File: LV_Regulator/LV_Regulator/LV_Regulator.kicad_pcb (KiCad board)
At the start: 4 copper layers, 150 x 100 mm, 190 parts, among them IC1 UCC12040DVE, IC2 MIC29152WU, IC3 MIC29152WU, J3 430450800, K1 41.52.9.005.0010, K1 REL, Q1 BC807, U1 ADM2483xRW, U2 STM32F103C8Tx, U3 25CSM04xxSN, U4 BQ25858QWRRVRQ1, U5 CSD19506KTT, U6 CSD19506KTT, U7 CSD19506KTT, U8 CSD19506KTT, Y1 32.768kHz, Y2 8MHz

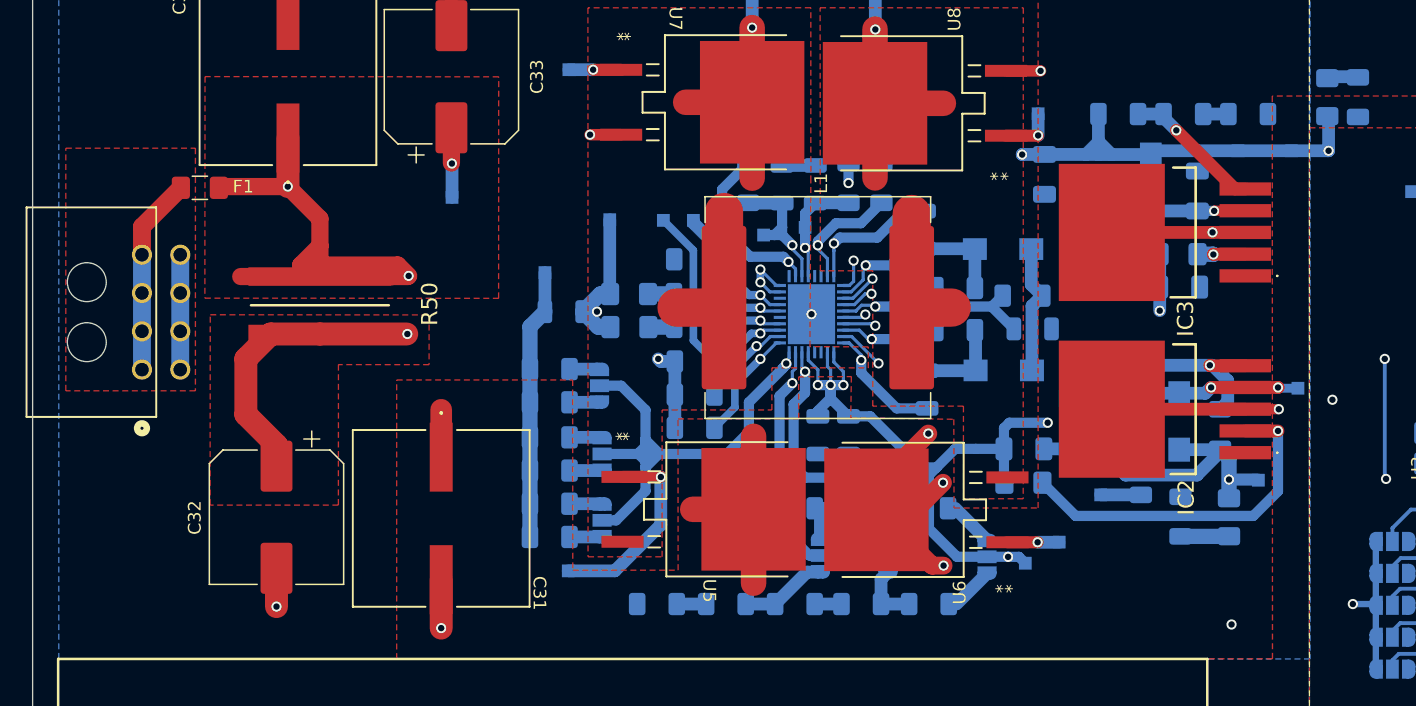
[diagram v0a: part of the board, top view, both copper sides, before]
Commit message: Fixed DRC & some other minor tweaks
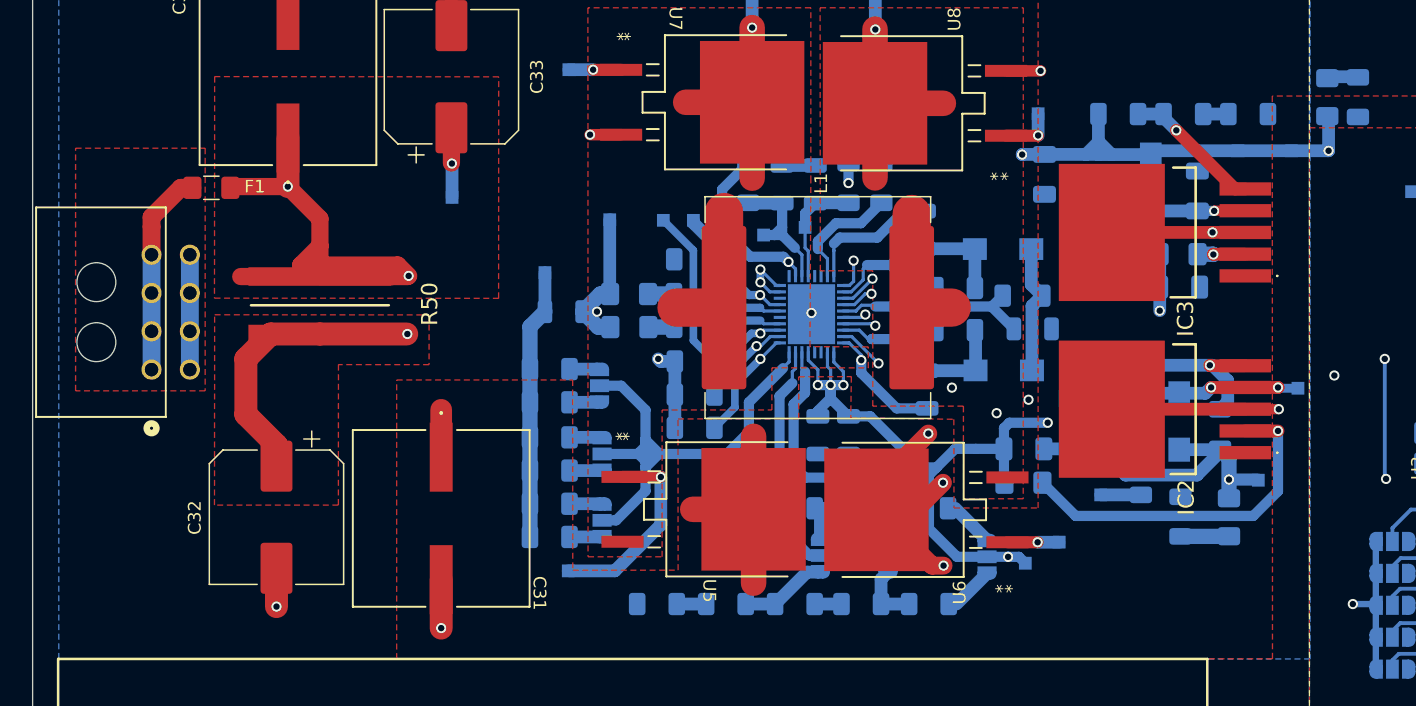
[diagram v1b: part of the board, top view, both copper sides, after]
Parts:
- moved F1 0.90 mm to (95.0, 75.1)
- moved J3 0.75 mm to (90.3, 89.3)
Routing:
- net CE_N: track 102.7 -> 93.9 mm
- net VOUT: track 67.9 -> 67.0 mm
- net Net-(F1-Pad2): track 15.5 -> 16.1 mm
- net I2C_SCL: track 82.9 -> 83.4 mm, vias 2 -> 4
- net BTST2: track 9.36 -> 9.34 mm, vias 1 -> 0
- net Izbor_frekvencije: vias 1 -> 0
- net SRN: vias 1 -> 0
- net SW2: vias 2 -> 1
- net SRP: vias 1 -> 0
- net Net-(U4-STAT): vias 1 -> 0
- net Net-(U4-PG_N): vias 1 -> 0
- net Net-(U4-MODE): vias 1 -> 0
- net DRV_SUPPLY: vias 1 -> 0
- net BTST1: vias 1 -> 0
- net ACUV: vias 1 -> 0
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
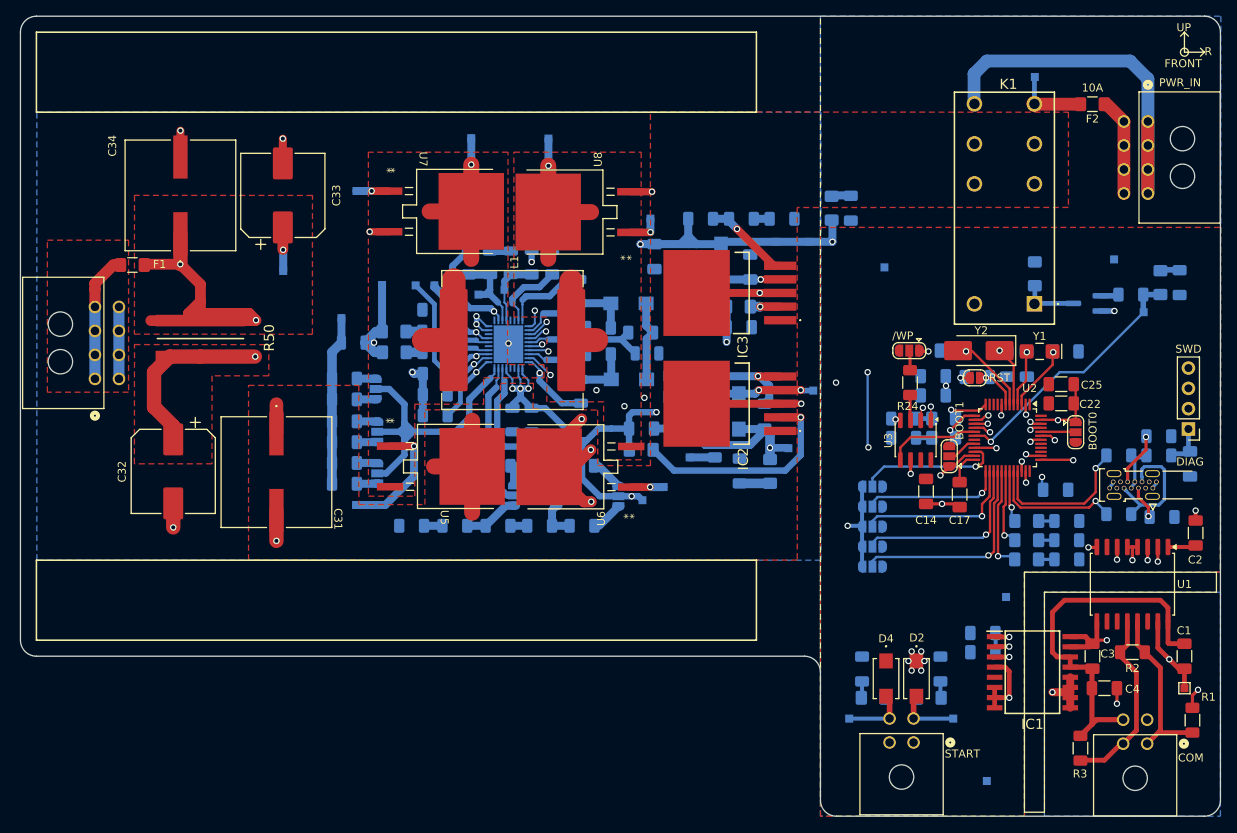
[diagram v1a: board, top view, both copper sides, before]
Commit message: PCB changes
Changes to the silkscreen of the pcb, added mounting holes, modified the schematic to comply with the template, more...
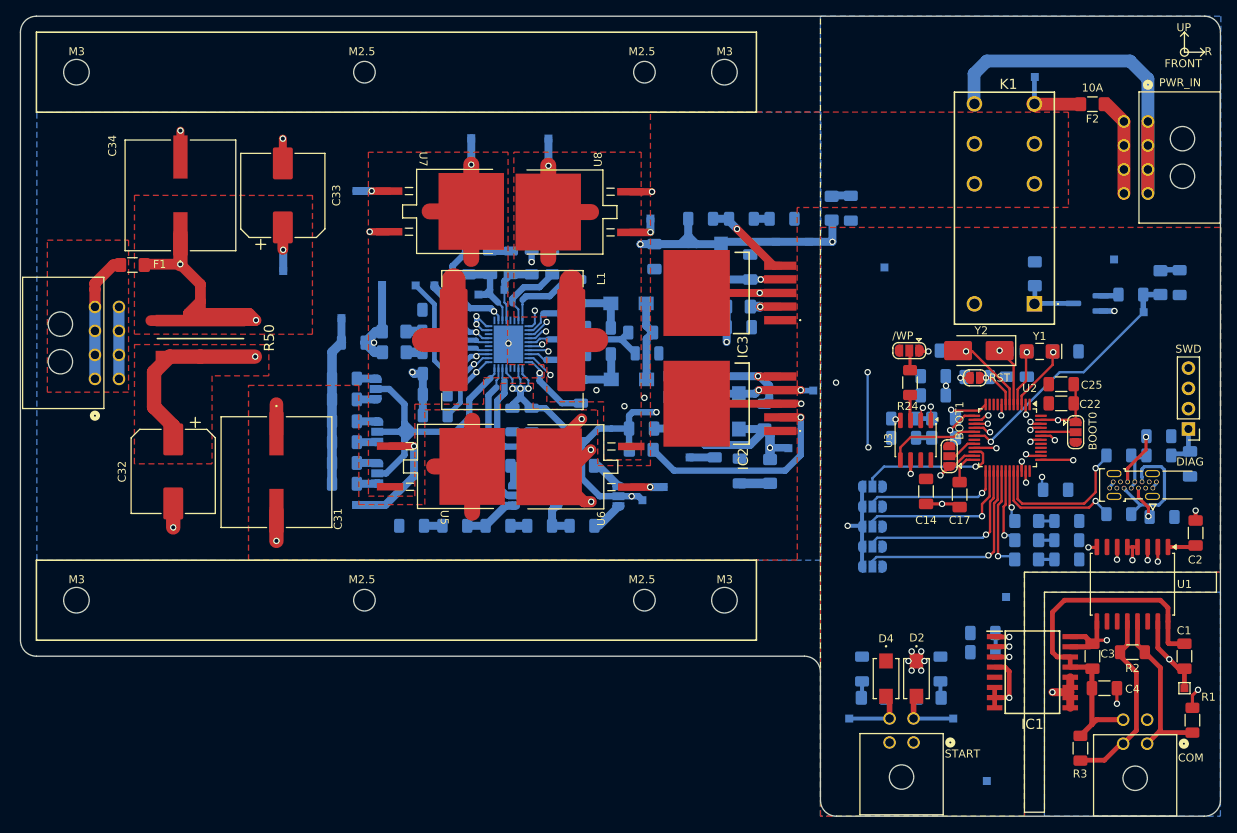
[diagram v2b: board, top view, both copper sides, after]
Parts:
- added REF**: MountingHole_2.7mm_M2.5, MountingHole:MountingHole_2.7mm_M2.5, F.Cu at (124.0, 51.0)
- added REF**: MountingHole_2.7mm_M2.5, MountingHole:MountingHole_2.7mm_M2.5, F.Cu at (159.0, 117.0)
- added REF**: MountingHole_3.2mm_M3, MountingHole:MountingHole_3.2mm_M3, F.Cu at (88.0, 117.0)
- added REF**: MountingHole_3.2mm_M3, MountingHole:MountingHole_3.2mm_M3, F.Cu at (88.0, 51.0)
- added REF**: MountingHole_2.7mm_M2.5, MountingHole:MountingHole_2.7mm_M2.5, F.Cu at (124.0, 117.0)
- added REF**: MountingHole_2.7mm_M2.5, MountingHole:MountingHole_2.7mm_M2.5, F.Cu at (159.0, 51.0)
- added REF**: MountingHole_3.2mm_M3, MountingHole:MountingHole_3.2mm_M3, F.Cu at (169.0, 51.0)
- added REF**: MountingHole_3.2mm_M3, MountingHole:MountingHole_3.2mm_M3, F.Cu at (169.0, 117.0)
- renumbered JP15 to ACOV, JP14 to ACUV, JP10 to FRQ2.5/4, JP11 to FRQ3/3.5, JP12 to FRQ5/4.5, JP13 to VIN12/48
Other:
- board text added: "M2.5"
- board text added: "M3"
- board text removed: "When selecting ACOV/ACUV input protection value, short ONLY one side either Left or Right. Input choices are: 19-48V - R39,R40,R41 12V - R32,R33,R34,R35,R36 For anything else look in manual"
- board text removed: "When selecting FSW value short ONLY 1 pad for 1 R Selectable frequencies: Rfsw1: 132k - R28 - 250kHZ Rfsw2: 100k - R30 - 300kHZ Rfsw3: 80k - R37 - 350kHZ Rfsw4: 67k - R29 - 400kHZ Rfsw5: 57k - R31 - 450kHZ Rfsw6: 50k - R38 - 500kHZ"

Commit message: Finished BoM Sheet, Fixed Component issues.
Fixed DRC Errors, as well as changing a Capacitor that was not chosen correctly. And have filled Bill of Materials.
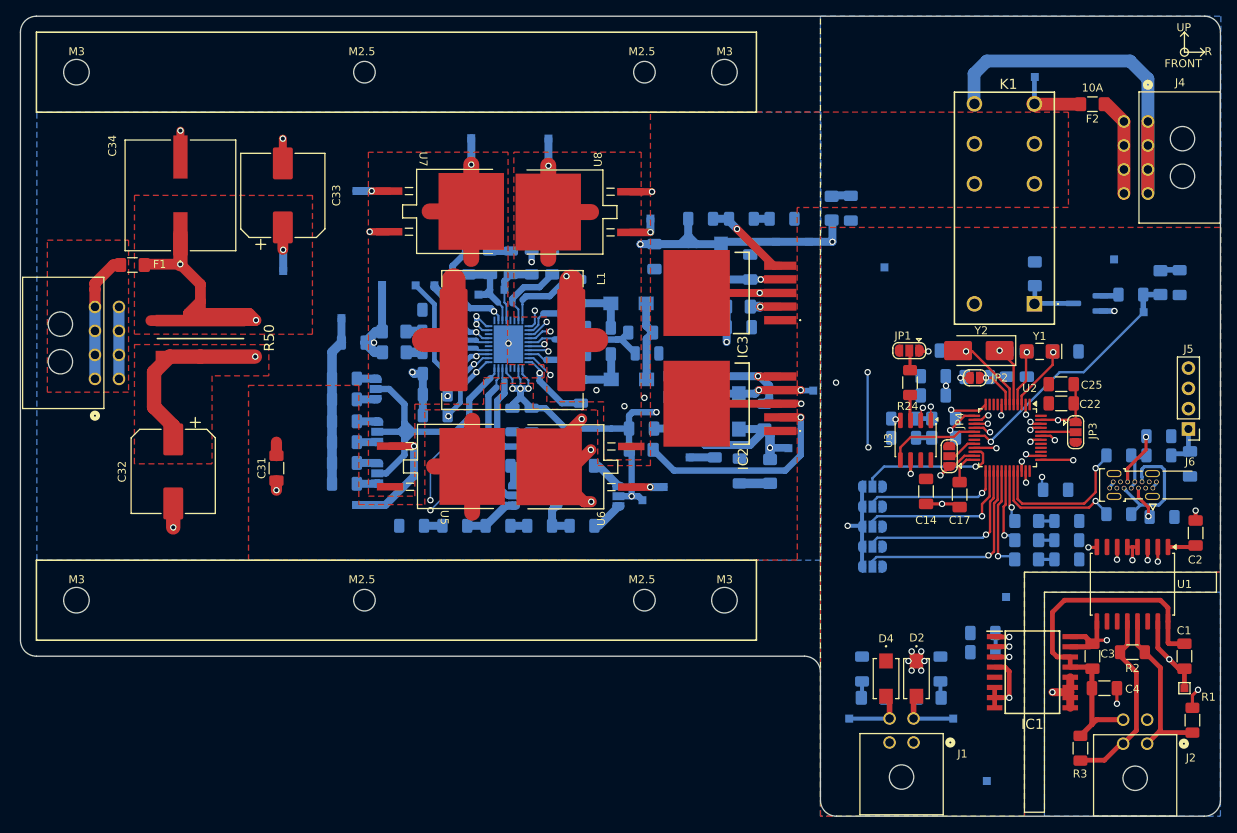
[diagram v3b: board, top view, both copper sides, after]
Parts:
- C31: footprint ul_UCZ1J181MNQ1MS:CAP_UCD_12P5X13P5_NCH -> Capacitor_SMD:C_1206_3216Metric_Pad1.33x1.80mm_HandSolder
- moved C31 0.50 mm to (113.0, 100.5), turned to 90 degrees
- renumbered START to J1, COM to J2, PWR_IN to J4, SWD to J5, DIAG to J6, /WP to JP1, FRQ2.5/4 to JP10, FRQ3/3.5 to JP11, FRQ5/4.5 to JP12, VIN12/48 to JP13, ACUV to JP14, ACOV to JP15, RST to JP2, BOOT0 to JP3, BOOT1 to JP4, ADR5 to JP5, ADR4 to JP6, ADR3 to JP7, ADR2 to JP8, ADR1 to JP9, 5V_INT to LED1, RX to LED10, TX to LED11, RUN to LED12, 3V3_INT to LED2, 5V_EXT to LED3, 3V3_EXT to LED4, K1 to LED5, 5V to LED6, 3V3 to LED7, OK to LED8, ERR to LED9
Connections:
- C31 pad 1: SYS -> GND
- C31 pad 2: GND -> SYS
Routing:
- net I2C_SDA: track 84.0 -> 107.0 mm, vias 3 -> 5
- net I2C_SCL: track 83.4 -> 102.8 mm, vias 4 -> 6
- net SYS: track 91.9 -> 81.4 mm
- net GND: track 129.6 -> 127.5 mm
- net SW2: track 41.5 -> 42.5 mm, vias 1 -> 2
- net LODRV1_FET2: track 56.4 -> 57.0 mm
- net REGN: track 38.9 -> 39.5 mm

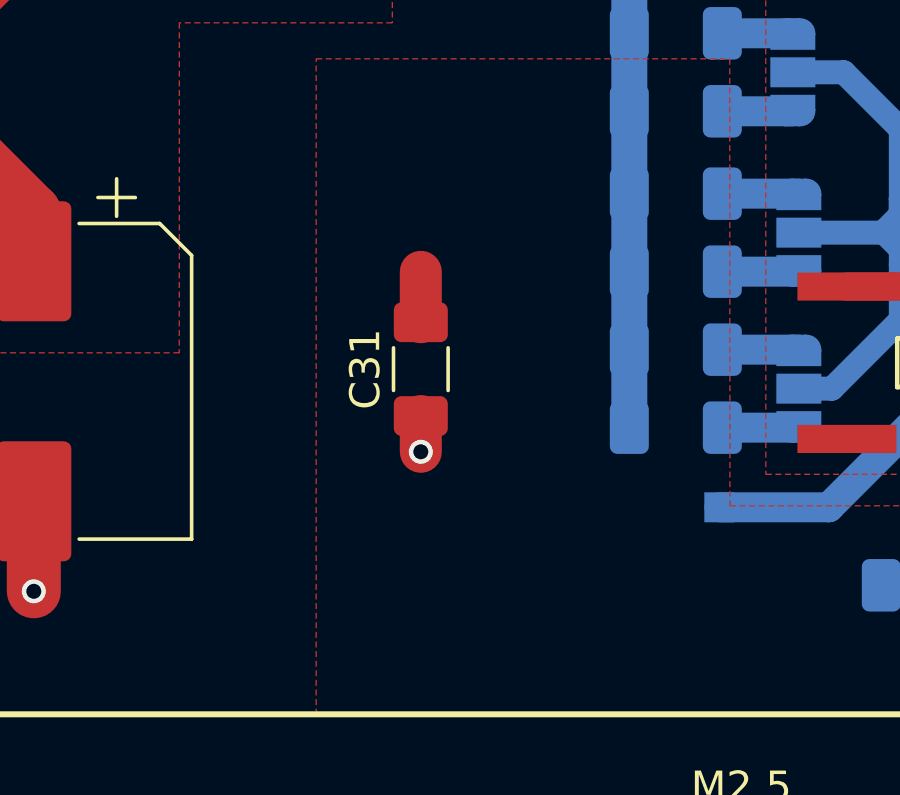
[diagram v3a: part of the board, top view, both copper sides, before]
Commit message: Fixed Capacitor choice
Mixed up Capacitor choices, fixed the issue
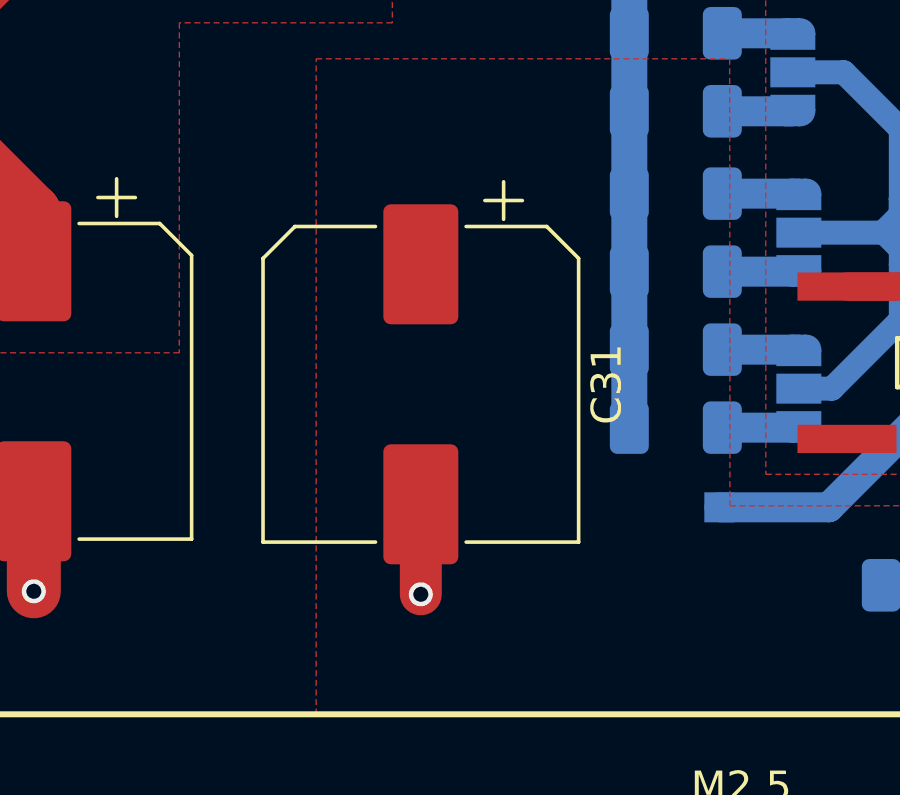
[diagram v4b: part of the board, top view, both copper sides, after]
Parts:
- C31: footprint Capacitor_SMD:C_1206_3216Metric_Pad1.33x1.80mm_HandSolder -> Capacitor_SMD:CP_Elec_10x10
- moved C31 0.50 mm to (113.0, 101.0), turned to -90 degrees
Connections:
- C31 pad 1: GND -> SYS
- C31 pad 2: SYS -> GND
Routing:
- net GND: track 127.5 -> 129.3 mm
- net SYS: track 81.4 -> 79.7 mm

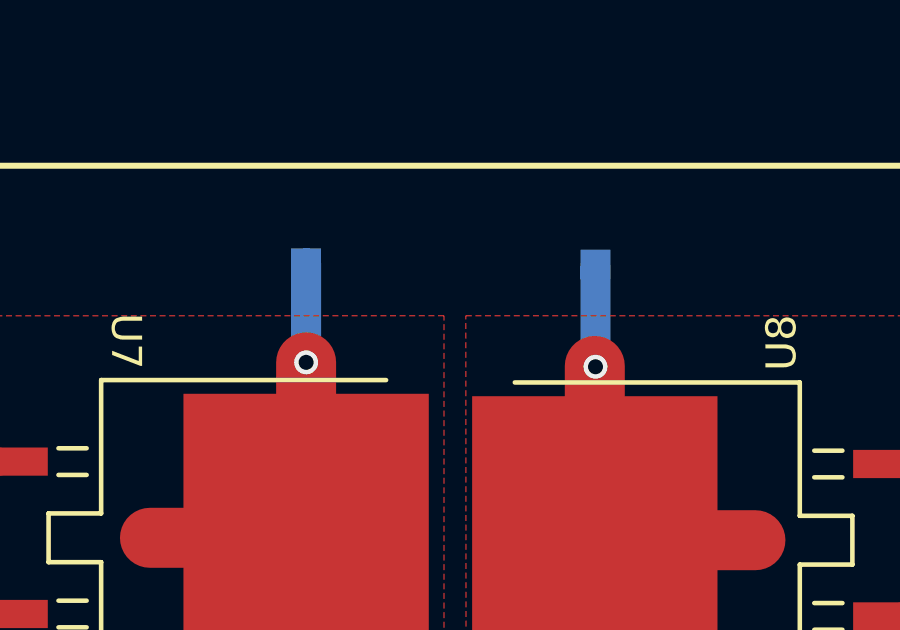
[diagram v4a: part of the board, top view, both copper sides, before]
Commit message: Added graphics to PCB
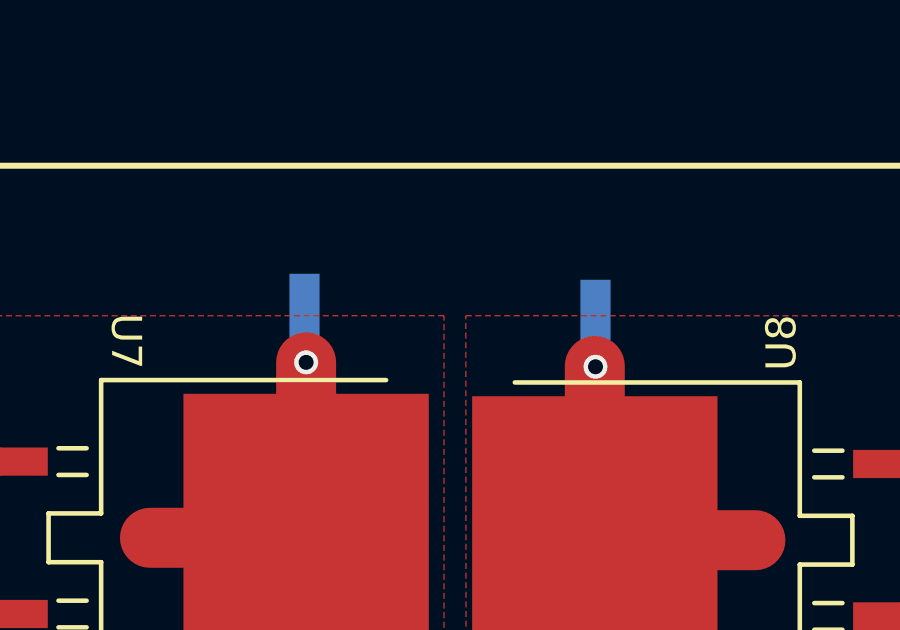
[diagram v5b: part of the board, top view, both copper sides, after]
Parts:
- added G***: LOGO, Graphics:FTN, B.Cu at (103.1, 62.1)
- added G***: LOGO, Graphics:Team, B.Cu at (91.8, 61.5)
- moved TP10 1.01 mm to (147.0, 60.3)
- moved TP9 0.85 mm to (137.3, 60.1)
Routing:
- net SW2: track 42.5 -> 41.6 mm
- net SW1: track 41.0 -> 40.2 mm
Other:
- board text added: "LV_Regulator - REV V01. Nikola Popovic, Dusan Novkovic Faculty of Technical Sciences Department of Power, Electronic and Telecommunication Engineering Programming:"
